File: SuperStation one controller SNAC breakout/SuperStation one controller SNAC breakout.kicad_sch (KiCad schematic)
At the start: 28 parts, among them J1 Conn_01x09_Socket, J2 Conn_01x09_Socket, J3 USB3_A, Q1 BSS138, Q2 BSS138, Q3 BSS138, Q4 BSS138, Q5 BSS138, Q6 BSS138, Q7 BSS138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

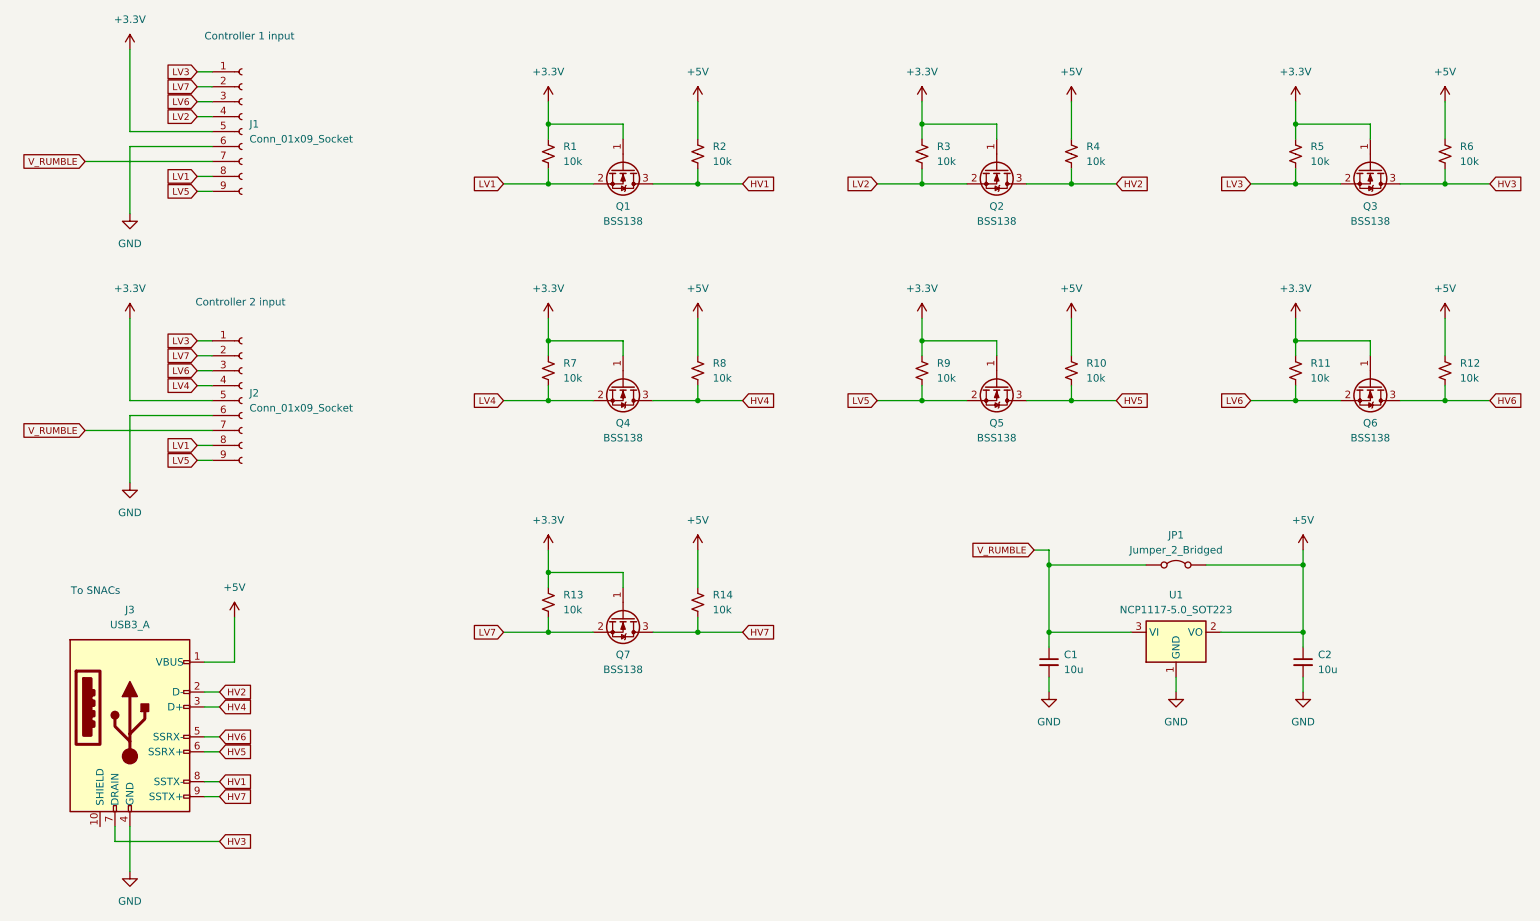
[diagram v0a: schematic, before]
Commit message: continued work on schematic. Added connector breakouts and muxing for 3.3v and 5v SNACs
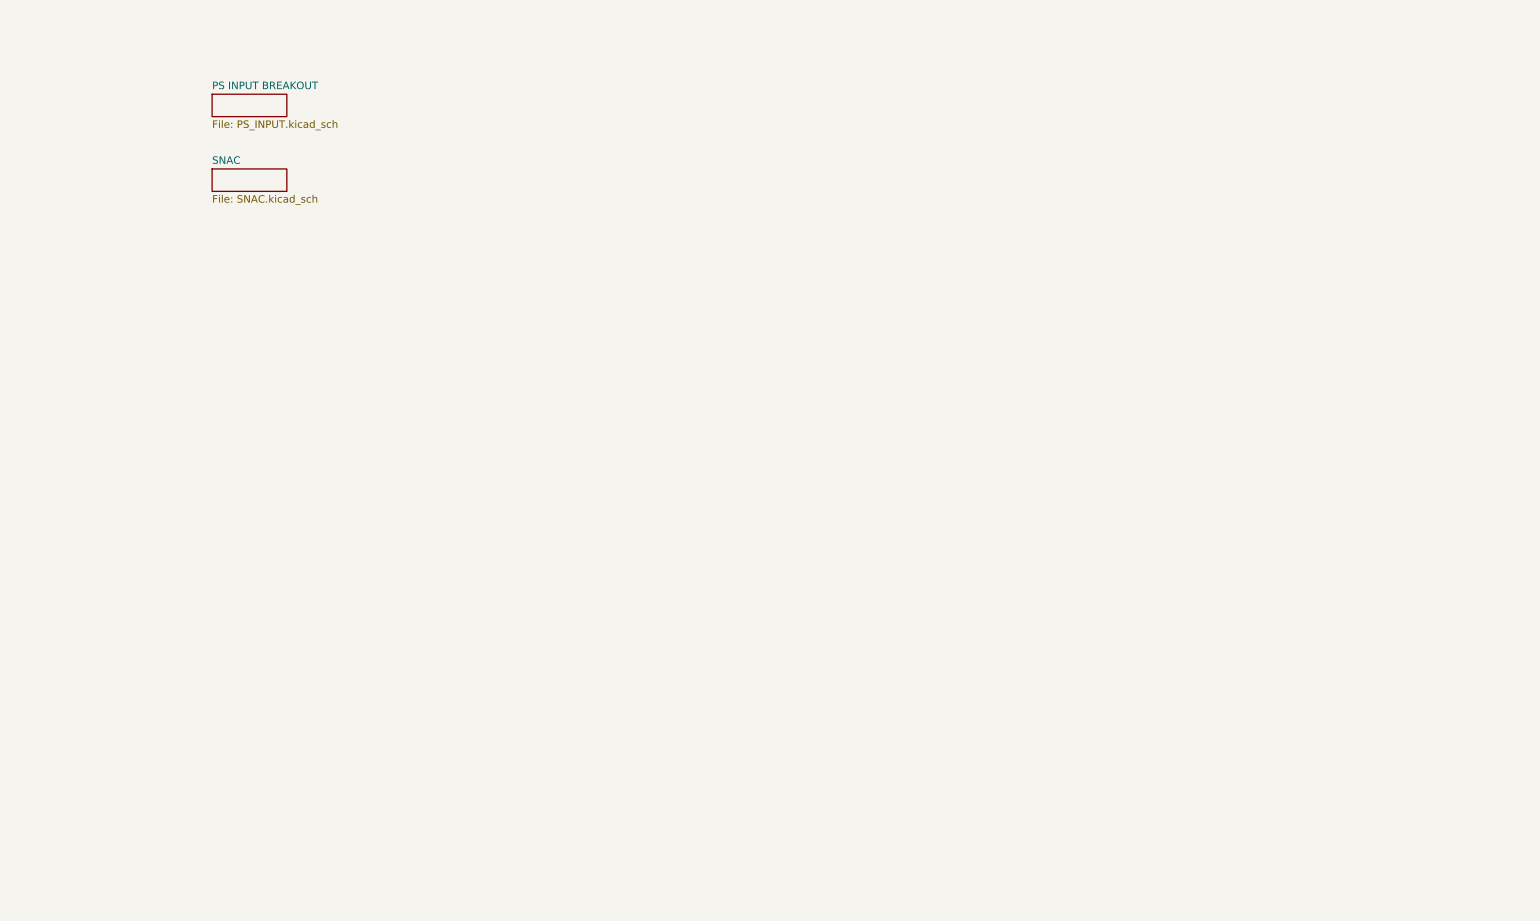
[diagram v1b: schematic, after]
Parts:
- removed C1, C2: 10u, Capacitor_SMD:C_0603_1608Metric, symbol Device:C_Small
- removed J1, J2: Conn_01x09_Socket, Connector_PinHeader_2.54mm:PinHeader_1x09_P2.54mm_Vertical, symbol Connector:Conn_01x09_Socket
- removed J3: USB3_A, Connector_USB:USB3_A_Receptacle_Wuerth_692122030100, symbol Connector:USB3_A
- removed JP1: Jumper_2_Bridged, Jumper:SolderJumper-2_P1.3mm_Bridged_Pad1.0x1.5mm, symbol Jumper:Jumper_2_Bridged
- removed Q1, Q2, Q3, Q4, Q5, Q6, Q7: BSS138, Package_TO_SOT_SMD:SOT-23, symbol Transistor_FET:BSS138
- removed R1, R10, R11, R12, R13, R14, R2, R3, R4, R5, R6, R7, R8, R9: 10k, Resistor_SMD:R_0603_1608Metric, symbol Device:R_Small_US
- removed U1: NCP1117-5.0_SOT223, Package_TO_SOT_SMD:SOT-223-3_TabPin2, symbol Regulator_Linear:NCP1117-5.0_SOT223
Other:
- added sheet PS INPUT BREAKOUT (PS_INPUT.kicad_sch)
- added sheet SNAC (SNAC.kicad_sch)
- note removed: "Controller 1 input"
- note removed: "Controller 2 input"
- note removed: "To SNACs"

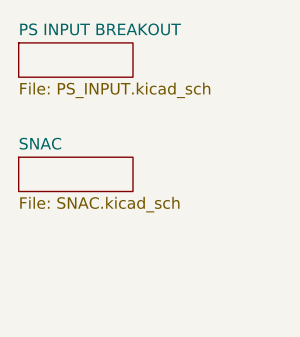
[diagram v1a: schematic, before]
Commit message: added power sheet to schematic and started rough pcb placement
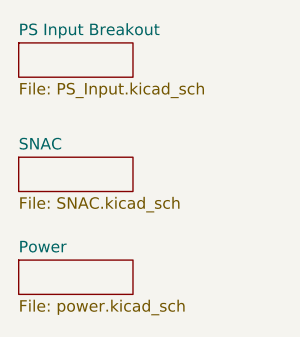
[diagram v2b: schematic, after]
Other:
- sheet PS INPUT BREAKOUT renamed PS Input Breakout
- added sheet Power (power.kicad_sch)
- sheet PS Input Breakout: file PS_INPUT.kicad_sch -> PS_Input.kicad_sch
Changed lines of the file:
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@@
 	(paper "B")
+	(sheet
+		(at 52.07 59.69)
+		(size 12.7 3.81)
+		(fields_autoplaced yes)
+		(stroke
+			(width 0.1524)
+			(type solid)
+		)
+		(fill
+			(color 0 0 0 0.0000)
+		)
+		(property "Sheetname" "Power"
+			(at 52.07 58.9784 0)
+			(effects
+				(font
+					(size 1.27 1.27)
+				)
+				(justify left bottom)
+			)
+		)
+		(property "Sheetfile" "power.kicad_sch"
+			(at 52.07 64.0846 0)
+			(effects
+				(font
+					(size 1.27 1.27)
+				)
+				(justify left top)
+			)
+		)
+		(instances
+			(project "SuperStation one controller SNAC breakout"
+				(path "/cbd92933-d20e-42b7-906c-813e5f34c94a"
+					(page "4")
+				)
+			)
+		)
+	)
 	(sheet
 		(at 52.07 35.56)
@@
 			(color 0 0 0 0.0000)
 		)
-		(property "Sheetname" "PS INPUT BREAKOUT"
+		(property "Sheetname" "PS Input Breakout"
 			(at 52.07 34.8484 0)
 			(effects
@@
 			)
 		)
-		(property "Sheetfile" "PS_INPUT.kicad_sch"
+		(property "Sheetfile" "PS_Input.kicad_sch"
 			(at 52.07 39.9546 0)
 			(effects
